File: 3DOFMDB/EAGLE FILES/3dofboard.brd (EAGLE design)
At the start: 83.2 x 80.1 mm, 163 parts, among them J2 M16DUAL_ROW, U1 DRV8312_DDW_44, U2 DRV8312_DDW_44, U3 DRV8312_DDW_44, U4 PIC32MZXXXXEC(G/H/M)100-I/PT

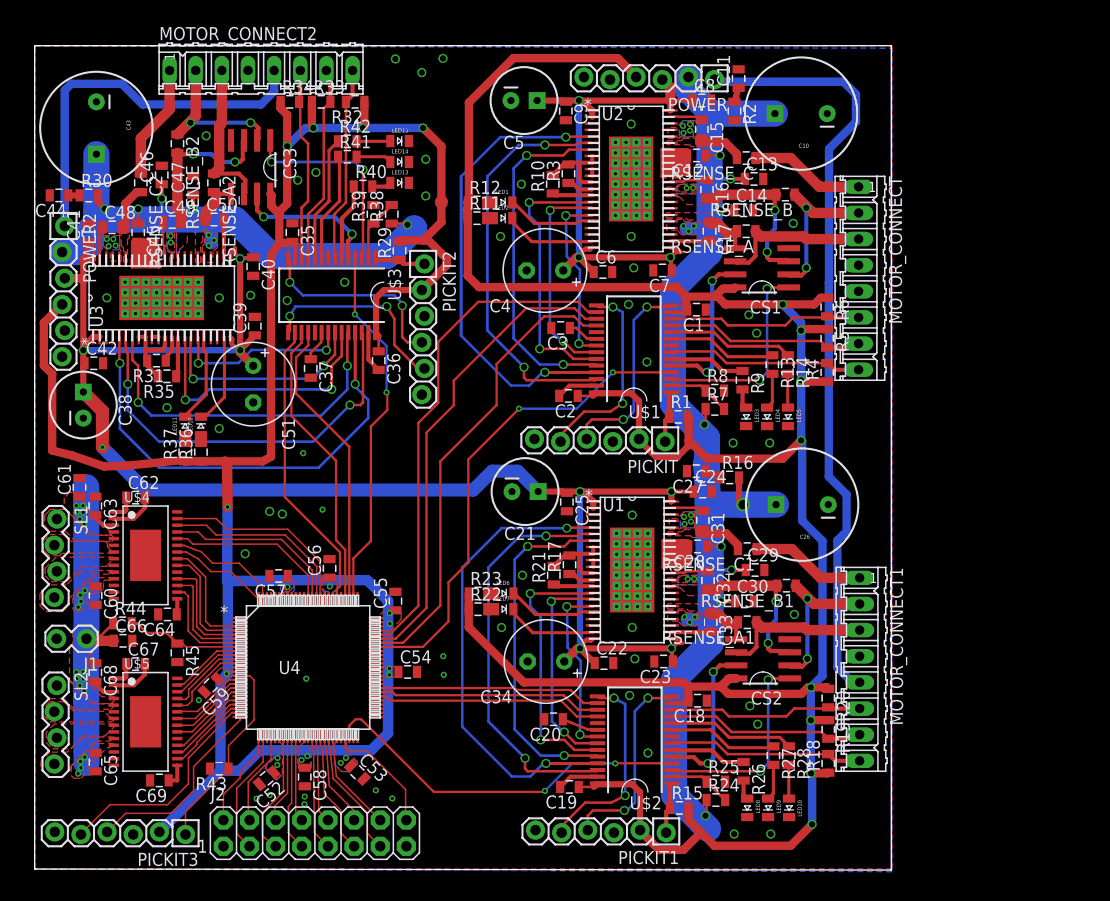
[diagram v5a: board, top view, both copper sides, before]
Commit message: Names, GND vias, Mounting holes
Moved the names around so they don't overlap, added a bunch of ground
vias (not very systematically), and 4 mounting holes in the corners (not
quite symmetrical)
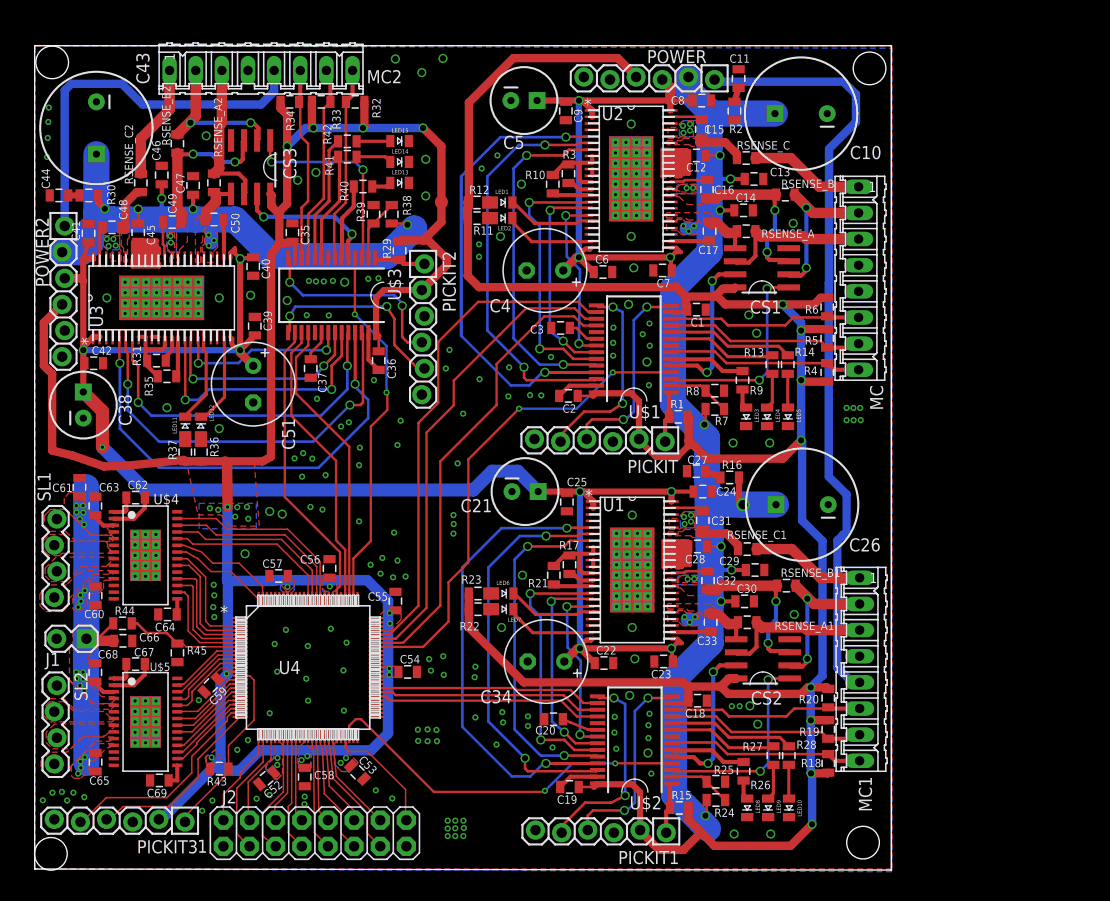
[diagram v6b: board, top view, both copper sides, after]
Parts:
- moved PICKIT3 1.22 mm to (14.6, 4.70)
- renumbered MOTOR_CONNECT to MC, MOTOR_CONNECT1 to MC1, MOTOR_CONNECT2 to MC2
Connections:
- net GND: now also U$4.P$1, U$4.P$10, U$4.P$11, U$4.P$12, U$4.P$13, U$4.P$14, U$4.P$15, U$4.P$16, U$4.P$2, U$4.P$3, U$4.P$4, U$4.P$5, U$4.P$6, U$4.P$7, U$4.P$8, U$4.P$9, U$5.P$1, U$5.P$10, U$5.P$11, U$5.P$12, U$5.P$13, U$5.P$14, U$5.P$15, U$5.P$16, U$5.P$2, U$5.P$3, U$5.P$4, U$5.P$5, U$5.P$6, U$5.P$7, U$5.P$8, U$5.P$9, U1.P$33, U2.P$33, U3.P$33
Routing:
- net MCLR_BP: track 19.3 -> 18.1 mm
- net PGD_BP: track 19.1 -> 18.2 mm
- net PGC_BP: track 21.9 -> 21.1 mm
- net 3V3: vias 26 -> 33
- net GND: vias 54 -> 175

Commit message: Filled out BOM with digikey parts
Except for what you can sample from microchip and TI
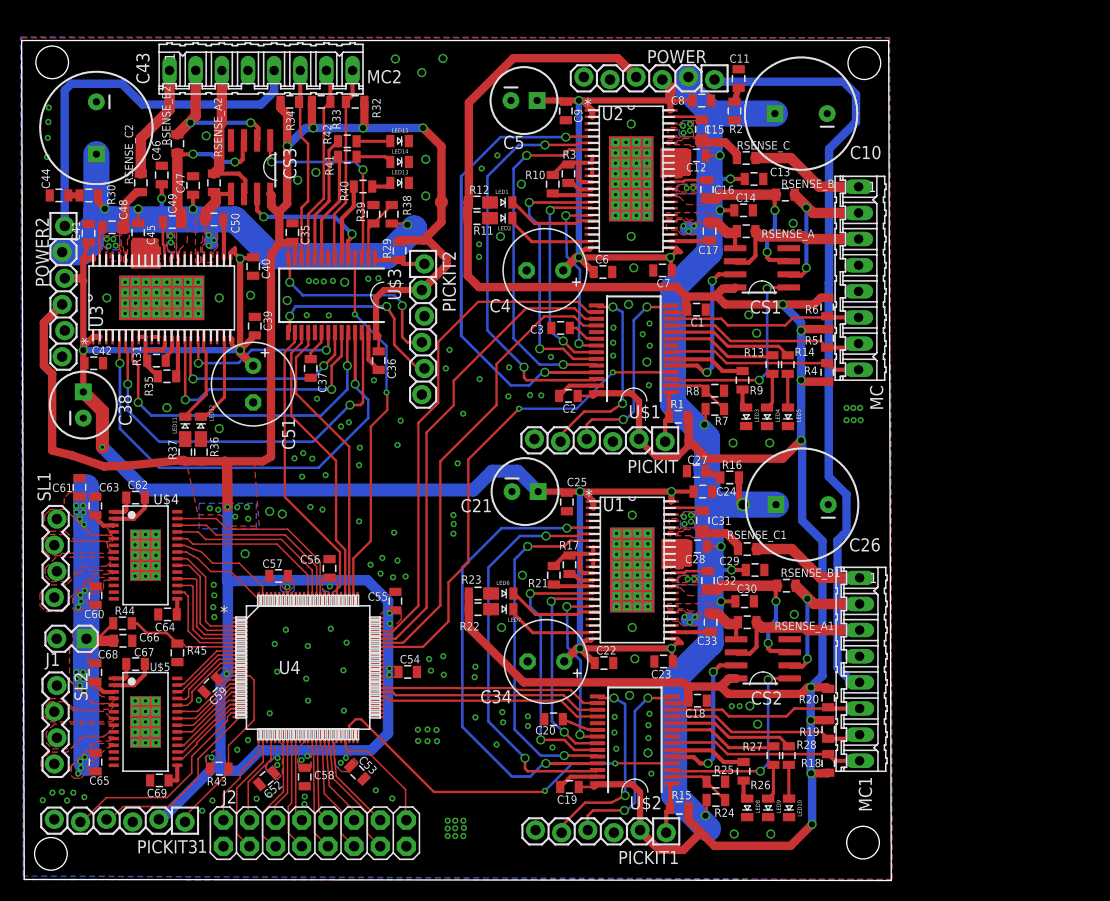
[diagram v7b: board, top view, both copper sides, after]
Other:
- board size 83.2 x 80.1 mm -> 84.5 x 81.6 mm
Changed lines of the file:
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@@
 <setting verticaltext="up"/>
 </settings>
-<grid distance="0.001" unitdist="inch" unit="inch" style="lines" multiple="1" display="no" altdistance="0.025" altunitdist="inch" altunit="inch"/>
+<grid distance="0.01" unitdist="inch" unit="inch" style="lines" multiple="1" display="no" altdistance="0.025" altunitdist="inch" altunit="inch"/>
 <layers>
 <layer number="1" name="Top" color="4" fill="1" visible="yes" active="yes"/>
@@
 <board>
 <plain>
-<wire x1="0" y1="0" x2="83.236" y2="-0.1016" width="0" layer="20"/>
-<wire x1="83.236" y1="-0.1016" x2="83.236" y2="80" width="0" layer="20"/>
-<wire x1="83.236" y1="80" x2="0" y2="80" width="0" layer="20"/>
-<wire x1="0" y1="80" x2="0" y2="0" width="0" layer="20"/>
-<hole x="81.1276" y="77.8002" drill="3.175"/>
+<wire x1="-1.016" y1="-1.016" x2="83.236" y2="-1.1176" width="0" layer="20"/>
+<wire x1="83.236" y1="-1.1176" x2="82.982" y2="80.508" width="0" layer="20"/>
+<wire x1="82.982" y1="80.508" x2="-1.27" y2="80.508" width="0" layer="20"/>
+<wire x1="-1.27" y1="80.508" x2="-1.016" y2="-1.016" width="0" layer="20"/>
+<hole x="80.6196" y="78.3082" drill="3.175"/>
 <hole x="80.4926" y="2.5654" drill="3.175"/>
 <hole x="1.7018" y="78.3844" drill="3.175"/>
@@
 <wire x1="63.6524" y1="29.5656" x2="63.6524" y2="30.8356" width="0.4064" layer="1"/>
 <polygon width="0.1524" layer="1" thermals="no" rank="6">
-<vertex x="0" y="0"/>
-<vertex x="0" y="80.01"/>
-<vertex x="83.312" y="80.01"/>
-<vertex x="83.312" y="0"/>
+<vertex x="-1.016" y="-1.016"/>
+<vertex x="-1.27" y="80.772"/>
+<vertex x="83.058" y="80.772"/>
+<vertex x="83.312" y="-1.016"/>
 </polygon>
 <polygon width="0.4064" layer="16" thermals="no" rank="6">
-<vertex x="0" y="0"/>
-<vertex x="0" y="80.01"/>
-<vertex x="83.312" y="79.756"/>
-<vertex x="83.312" y="-0.254"/>
+<vertex x="-1.1176" y="-0.6858"/>
+<vertex x="-1.3716" y="80.8482"/>
+<vertex x="83.058" y="80.772"/>
+<vertex x="83.312" y="-1.016"/>
 </polygon>
 <contactref element="U$3" pad="8"/>

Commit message: Moved the DSPIC33 library into the github repo
yup, that's it
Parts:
- U$1, U$2, U$3: device microchip:SSOP28 -> DSPIC33:SSOP28
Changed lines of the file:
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@@
 </element>
 <element name="CS1" library="3DOFMDB_COMPONENTS" package="SO8" value="MAX4376" x="70.6628" y="58.42" rot="R90"/>
-<element name="U$1" library="microchip" package="SSOP28" value="" x="58.2168" y="50.546" rot="R90">
+<element name="U$1" library="DSPIC33" package="SSOP28" value="" x="58.2168" y="50.546" rot="R90">
 <attribute name="DSPIC33EP512MC502" value="" x="58.2168" y="50.546" size="1.778" layer="27" rot="R90" display="off"/>
 </element>
@@
 </element>
 <element name="CS2" library="3DOFMDB_COMPONENTS" package="SO8" value="MAX4376" x="70.7644" y="20.4216" rot="R90"/>
-<element name="U$2" library="microchip" package="SSOP28" value="" x="58.3184" y="12.5476" rot="R90">
+<element name="U$2" library="DSPIC33" package="SSOP28" value="" x="58.3184" y="12.5476" rot="R90">
 <attribute name="DSPIC33EP512MC502" value="" x="58.3184" y="12.5476" size="1.778" layer="27" rot="R90" display="off"/>
 </element>
@@
 </element>
 <element name="CS3" library="3DOFMDB_COMPONENTS" package="SO8" value="MAX4376" x="20.9804" y="68.199" rot="R180"/>
-<element name="U$3" library="microchip" package="SSOP28" value="" x="28.8544" y="55.753" rot="R180">
+<element name="U$3" library="DSPIC33" package="SSOP28" value="" x="28.8544" y="55.753" rot="R180">
 <attribute name="DSPIC33EP512MC502" value="" x="28.8544" y="55.753" size="1.778" layer="27" rot="R180" display="off"/>
 </element>
